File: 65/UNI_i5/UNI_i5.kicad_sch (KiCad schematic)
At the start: 191 parts, among them J2 Conn_01x04, J3 Conn_01x05, SW1 MX_SW_solder, SW10 MX_SW_solder, SW11 MX_SW_solder, SW12 MX_SW_solder, SW13 MX_SW_solder, SW14 MX_SW_solder, SW15 MX_SW_solder, SW16 MX_SW_solder, SW17 MX_SW_solder, SW18 MX_SW_solder, SW19 MX_SW_solder, SW2 MX_SW_solder, SW20 MX_SW_solder, SW21 MX_SW_solder, SW22 MX_SW_solder, SW23 MX_SW_solder, SW24 MX_SW_solder, SW25 MX_SW_solder, SW26 MX_SW_solder, SW27 MX_SW_solder, SW28 MX_SW_solder, SW29 MX_SW_solder, SW3 MX_SW_solder, SW30 MX_SW_solder, SW31 MX_SW_solder, SW32 RotaryEncoder_Switch, SW33 MX_SW_solder, SW34 MX_SW_solder, SW35 MX_SW_solder, SW36 MX_SW_solder, SW37 MX_SW_solder, SW38 MX_SW_solder, SW39 MX_SW_solder, SW4 MX_SW_solder, SW40 MX_SW_solder, SW41 MX_SW_solder, SW42 MX_SW_solder, SW43 MX_SW_solder, SW44 MX_SW_solder, SW45 MX_SW_solder, SW46 MX_SW_solder, SW47 MX_SW_solder, SW48 RotaryEncoder_Switch, SW49 MX_SW_solder, SW5 MX_SW_solder, SW50 MX_SW_solder, SW51 MX_SW_solder, SW52 MX_SW_solder, SW53 MX_SW_solder, SW54 MX_SW_solder, SW55 MX_SW_solder, SW56 MX_SW_solder, SW57 MX_SW_solder, SW58 MX_SW_solder, SW59 MX_SW_solder, SW6 MX_SW_solder, SW60 MX_SW_solder, SW61 MX_SW_solder, SW62 MX_SW_solder, SW63 MX_SW_solder, SW64 MX_SW_solder, SW65 MX_SW_solder, SW66 MX_SW_solder, SW67 MX_SW_solder, SW68 MX_SW_solder, SW69 MX_SW_solder, SW7 MX_SW_solder, SW70 MX_SW_solder, SW71 MX_SW_solder, SW72 MX_SW_solder, SW73 MX_SW_solder, SW74 MX_SW_solder, SW75 MX_SW_solder, SW76 SW_RESET, SW77 SW_BOOTSEL, SW8 MX_SW_solder, SW9 MX_SW_solder, U1 RP2040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

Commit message: 65 v3
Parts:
- removed J2: Conn_01x04, Connector_Molex:Molex_Pico-EZmate_78171-0004_1x04-1MP_P1.20mm_Vertical, symbol Connector_Generic:Conn_01x04
- added F1: Fuse_Small, Fuse:Fuse_1206_3216Metric, symbol Device:Fuse_Small
- added P1: USB_C_Plug_USB2.0, Connector_USB:USB_C_Receptacle_HRO_TYPE-C-31-M-12, symbol Connector:USB_C_Plug_USB2.0
- added R1, R2: 5.1k, Resistor_SMD:R_0402_1005Metric, symbol Device:R_Small
- added U3: SRV05-4, PCM_marbastlib-various:SOT-23-6-routable, symbol PCM_marbastlib-various:SRV05-4
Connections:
- net +5V: now also F1.2, U3.5 (VP)
- net D+: now also P1.A6 (D+), U3.1 (IO1)
- net D-: now also P1.A7 (D-), U3.6 (IO4)
- net GND: now also P1.A1 (GND), P1.A12 (GND), P1.B1 (GND), P1.B12 (GND), P1.S1 (SHIELD), R1.1, R2.1, U3.2 (VN)
- new net: F1.1, P1.A4 (VBUS), P1.A9 (VBUS), P1.B4 (VBUS), P1.B9 (VBUS)
- new net: P1.B5 (VCONN), R2.2
- new net: P1.A5 (CC), R1.2

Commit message: v4
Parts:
- removed F1: Fuse_Small, Fuse:Fuse_1206_3216Metric, symbol Device:Fuse_Small
- removed P1: USB_C_Plug_USB2.0, Connector_USB:USB_C_Receptacle_HRO_TYPE-C-31-M-12, symbol Connector:USB_C_Plug_USB2.0
- removed R1, R2: 5.1k, Resistor_SMD:R_0402_1005Metric, symbol Device:R_Small
- removed U3: SRV05-4, PCM_marbastlib-various:SOT-23-6-routable, symbol PCM_marbastlib-various:SRV05-4
- added J1: ZX-SH1.0-4PWT, Connector_JST:JST_SH_SM04B-SRSS-TB_1x04-1MP_P1.00mm_Horizontal, symbol Connector_Generic_MountingPin:Conn_01x04_MountingPin
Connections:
- net +5V: now also J1.1 (Pin_1)
- net D+: now also J1.3 (Pin_3)
- net D-: now also J1.2 (Pin_2)
- net GND: now also J1.4 (Pin_4), J1.MP (MountPin)
- net SW32A: now also U1.18 (GPIO15)
- net SW32B: now also U1.17 (GPIO14)
- net SW48A: now also U1.16 (GPIO13)
- net SW48B: now also U1.15 (GPIO12)

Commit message: uni tako icons
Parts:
- added H5: info, shoonies_parts:info, symbol Mechanical:MountingHole
- added H6: bottom row guide, shoonies_parts:bottom_row_guide, symbol Mechanical:MountingHole
- added H7: MountingHole_Pad, MountingHole:MountingHole_6mm_Pad, symbol Mechanical:MountingHole_Pad
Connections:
- net GND: now also H7.1
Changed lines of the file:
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@@
+    )
+  )
+  (symbol (lib_id "Mechanical:MountingHole_Pad") (at 264.16 166.37 270) (unit 1)
+    (in_bom yes) (on_board yes) (dnp no) (fields_autoplaced)
+    (property "Reference" "H7" (at 267.97 165.7263 90)
+      (effects (font (size 1.27 1.27)) (justify left))
+    )
+    (property "Value" "MountingHole_Pad" (at 267.97 167.6473 90)
+      (effects (font (size 1.27 1.27)) (justify left))
+    )
+    (property "Footprint" "MountingHole:MountingHole_6mm_Pad" (at 264.16 166.37 0)
+      (effects (font (size 1.27 1.27)) hide)
+    )
+    (property "Datasheet" "~" (at 264.16 166.37 0)
+      (effects (font (size 1.27 1.27)) hide)
+    )
+    (pin "1")
+    (instances
+      (project "UNI_i5"
+        (path "/2cf6646f-26e0-435f-a6db-0d19cf4986ba"
+          (reference "H7") (unit 1)
+        )
+      )
+      (project "UNI_i3"
+        (path "/6059e08a-17a3-445e-9a30-384483938524"
+          (reference "H4") (unit 1)
+        )
+      )
     )
   )
@@
         (path "/6059e08a-17a3-445e-9a30-384483938524"
           (reference "D3") (unit 1)
+        )
+      )
+    )
+  )
+  (symbol (lib_id "Mechanical:MountingHole") (at 265.43 179.07 0) (unit 1)
+    (in_bom yes) (on_board yes) (dnp no) (fields_autoplaced)
+    (property "Reference" "H5" (at 267.97 178.4263 0)
+      (effects (font (size 1.27 1.27)) (justify left))
+    )
+    (property "Value" "info" (at 267.97 180.3473 0)
+      (effects (font (size 1.27 1.27)) (justify left))
+    )
+    (property "Footprint" "shoonies_parts:info" (at 265.43 179.07 0)
+      (effects (font (size 1.27 1.27)) hide)
+    )
+    (property "Datasheet" "~" (at 265.43 179.07 0)
+      (effects (font (size 1.27 1.27)) hide)
+    )
+    (instances
+      (project "UNI_i5"
+        (path "/2cf6646f-26e0-435f-a6db-0d19cf4986ba"
+          (reference "H5") (unit 1)
+        )
+      )
+    )
+  )
+  (symbol (lib_id "Mechanical:MountingHole") (at 265.43 184.15 0) (unit 1)
+    (in_bom yes) (on_board yes) (dnp no) (fields_autoplaced)
+    (property "Reference" "H6" (at 267.97 183.5063 0)
+      (effects (font (size 1.27 1.27)) (justify left))
+    )
+    (property "Value" "bottom row guide" (at 267.97 185.4273 0)
+      (effects (font (size 1.27 1.27)) (justify left))
+    )
+    (property "Footprint" "shoonies_parts:bottom_row_guide" (at 265.43 184.15 0)
+      (effects (font (size 1.27 1.27)) hide)
+    )
+    (property "Datasheet" "~" (at 265.43 184.15 0)
+      (effects (font (size 1.27 1.27)) hide)
+    )
+    (instances
+      (project "UNI_i5"
+        (path "/2cf6646f-26e0-435f-a6db-0d19cf4986ba"
+          (reference "H6") (unit 1)
         )
       )
@@
         )
       )
+    )
+  )
+  (symbol (lib_id "power:GND") (at 261.62 166.37 270) (unit 1)
+    (in_bom yes) (on_board yes) (dnp no) (fields_autoplaced)
+    (property "Reference" "#PWR05" (at 255.27 166.37 0)
+      (effects (font (size 1.27 1.27)) hide)
+    )
+    (property "Value" "GND" (at 258.4451 166.6868 90)
+      (effects (font (size 1.27 1.27)) (justify right))
+    )
+    (property "Footprint" "" (at 261.62 166.37 0)
+      (effects (font (size 1.27 1.27)) hide)
+    )
+    (property "Datasheet" "" (at 261.62 166.37 0)
+      (effects (font (size 1.27 1.27)) hide)
+    )
+    (pin "1")
+    (instances
+      (project "UNI_i5"
+        (path "/2cf6646f-26e0-435f-a6db-0d19cf4986ba"
+          (reference "#PWR05") (unit 1)
+        )
+      )
+      (project "UNI_i3"
+        (path "/6059e08a-17a3-445e-9a30-384483938524"
+          (reference "#PWR012") (unit 1)
+        )
+      )

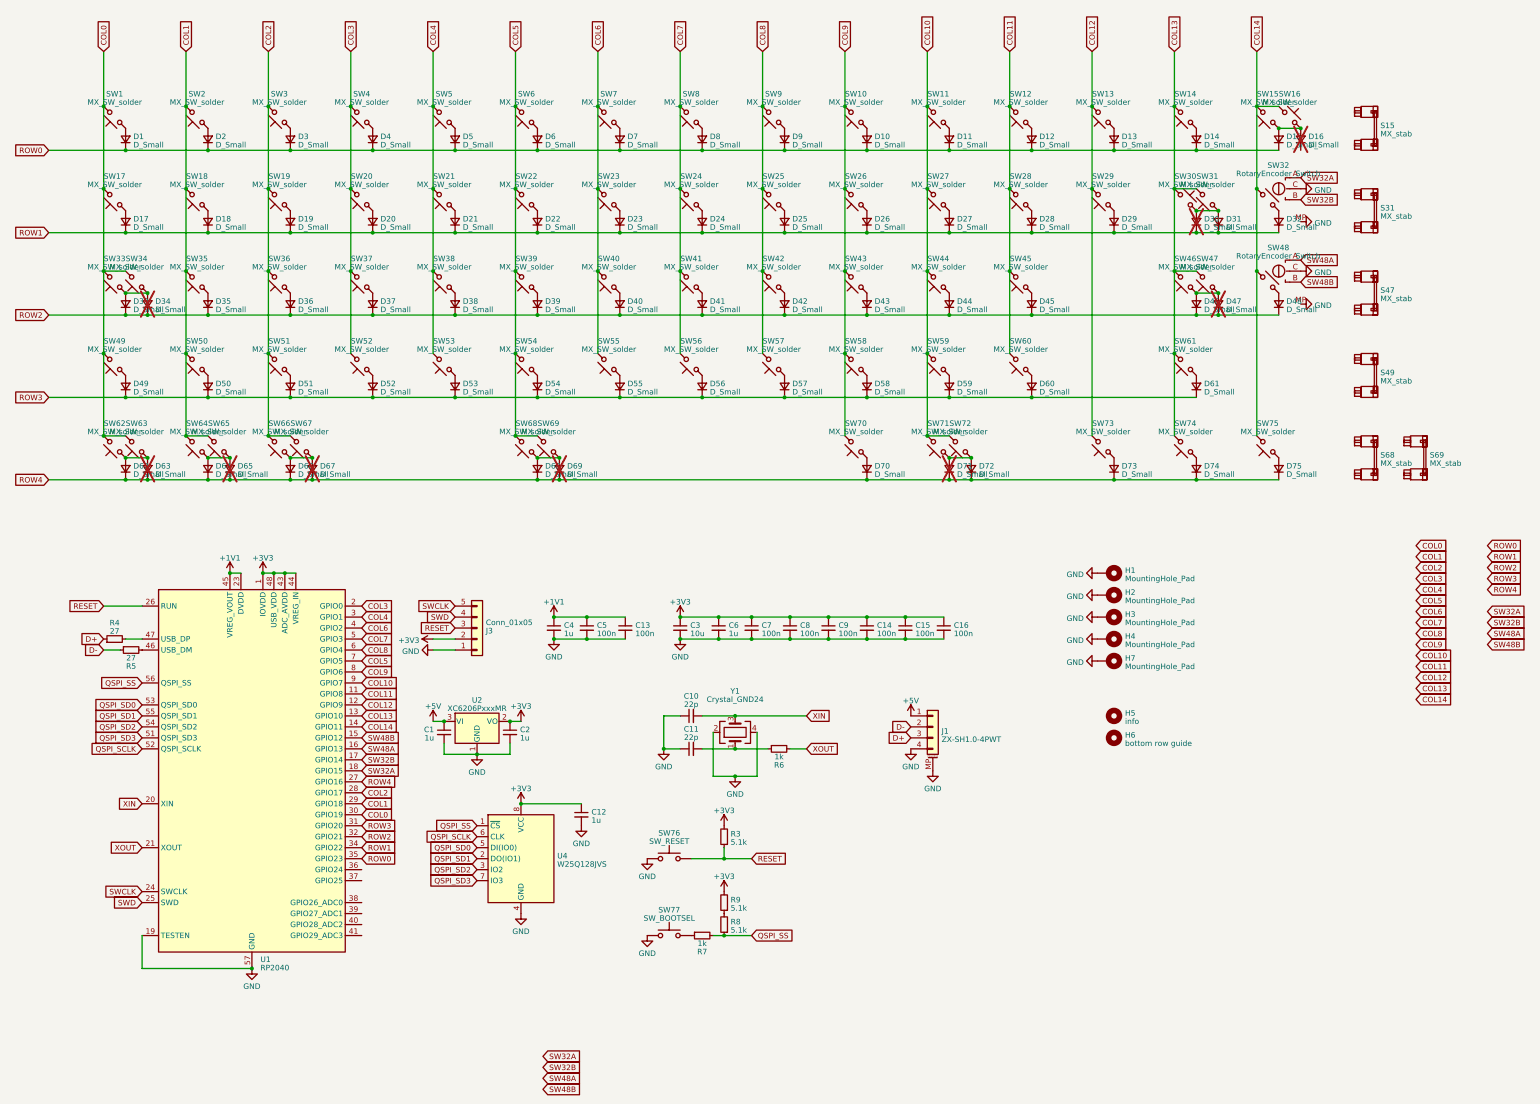
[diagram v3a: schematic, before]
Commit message: i5v5
split backspace
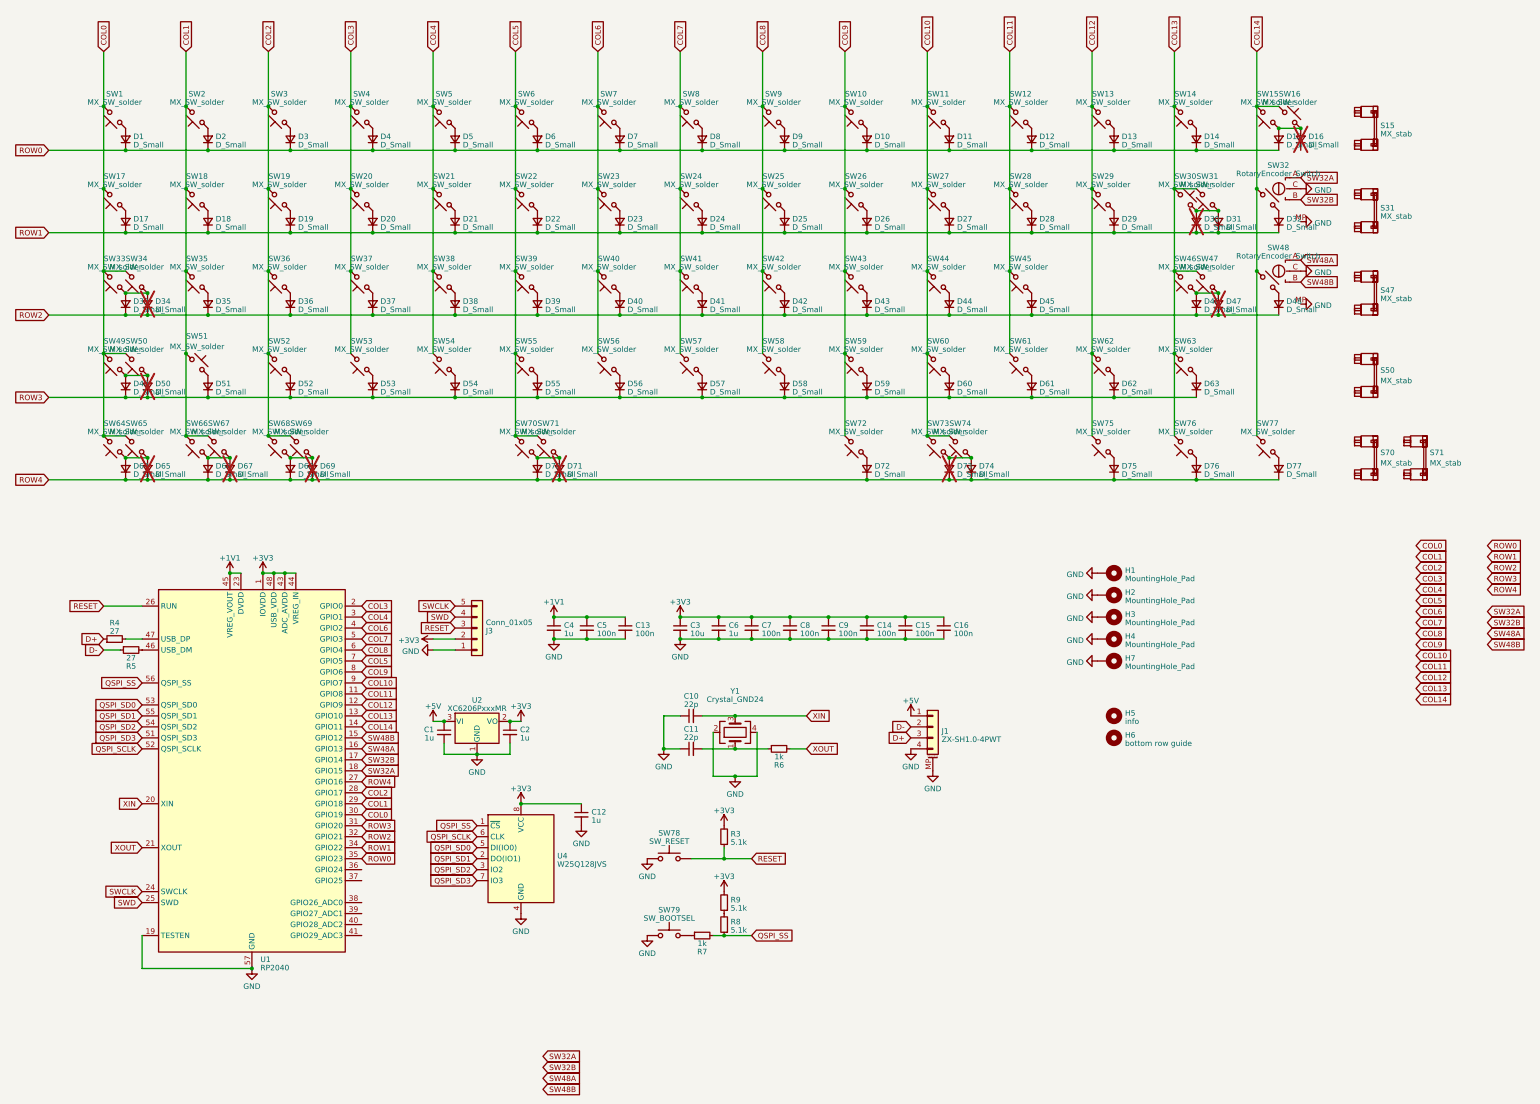
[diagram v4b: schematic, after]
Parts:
- added D50, D62: D_Small, shoonies_parts:D_SOD-123_CLEAN, symbol Device:D_Small
- added SW50, SW62: MX_SW_solder, PCM_marbastlib-mx:SW_MX_1u, symbol PCM_marbastlib-mx:MX_SW_solder
- J3, S15, S31, S47: now left out of the parts list
- S50: renamed from S49; now left out of the parts list
- S70: renamed from S68; now left out of the parts list
- S71: renamed from S69; now left out of the parts list
- SW78: renamed from SW76; now left out of the parts list
- SW79: renamed from SW77; now left out of the parts list
- renumbered D50 to D51, D51 to D52, D52 to D53, D53 to D54, D54 to D55, D55 to D56, D56 to D57, D57 to D58, D58 to D59, D59 to D60, D60 to D61, D61 to D63, D62 to D64, D63 to D65, D64 to D66, D65 to D67, D66 to D68, D67 to D69, D68 to D70, D69 to D71, D70 to D72, D71 to D73, D72 to D74, D73 to D75, D74 to D76, D75 to D77, SW50 to SW51, SW51 to SW52, SW52 to SW53, SW53 to SW54, SW54 to SW55, SW55 to SW56, SW56 to SW57, SW57 to SW58, SW58 to SW59, SW59 to SW60, SW60 to SW61, SW61 to SW63, SW62 to SW64, SW63 to SW65, SW64 to SW66, SW65 to SW67, SW66 to SW68, SW67 to SW69, SW68 to SW70, SW69 to SW71, SW70 to SW72, SW71 to SW73, SW72 to SW74, SW73 to SW75, SW74 to SW76, SW75 to SW77
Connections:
- net COL0: now also SW50.2
- net COL1: now also SW51.1; no longer SW51.2
- net COL12: now also SW62.2
- net ROW3: now also D50.1 (K), D62.1 (K)
- net at D51.2 (A): now also SW51.2; no longer SW51.1
- net at D49.2 (A), SW49.1: now also D50.2 (A), SW50.1
- new net: D62.2 (A), SW62.1
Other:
- moved on the sheet: SW51
